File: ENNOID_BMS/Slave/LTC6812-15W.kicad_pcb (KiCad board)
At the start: 2 copper layers, 66 x 91.2 mm, 247 parts, among them J1 PB MB 2, J10 PB MB 1, J11 PA MA 1, J2 PA MA 2, J3 Sensors, J5 Cells, J6 Sensors, Q1 DZTT5551, Q10 TSM2323, Q11 TSM2323, Q12 TSM2323, Q13 TSM2323, Q14 TSM2323, Q15 TSM2323, Q16 TSM2323, Q17 DZTT5551, Q18 2N7002, Q19 2N7002, Q2 TSM2323, Q20 2N7002, Q21 2N7002, Q22 2N7002, Q23 2N7002, Q24 2N7002, Q25 2N7002, Q26 2N7002, Q27 2N7002, Q28 2N7002, Q29 2N7002, Q3 TSM2323, Q30 2N7002, Q31 2N7002, Q32 2N7002, Q4 TSM2323, Q5 TSM2323, Q6 TSM2323, Q7 TSM2323, Q8 TSM2323, Q9 TSM2323, U1 LTC6812-1, U2 LTC6812-1

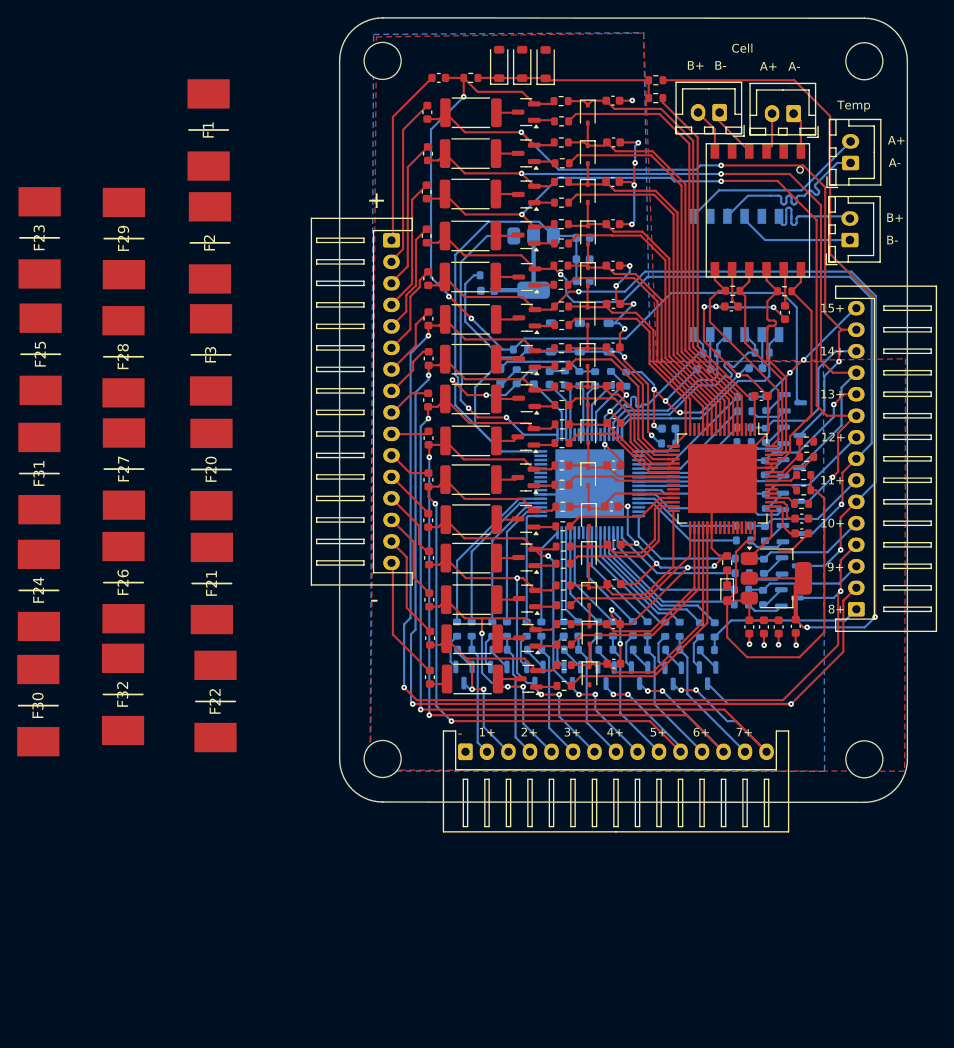
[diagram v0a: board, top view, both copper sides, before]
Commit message: Slave with SMD and no other fuses
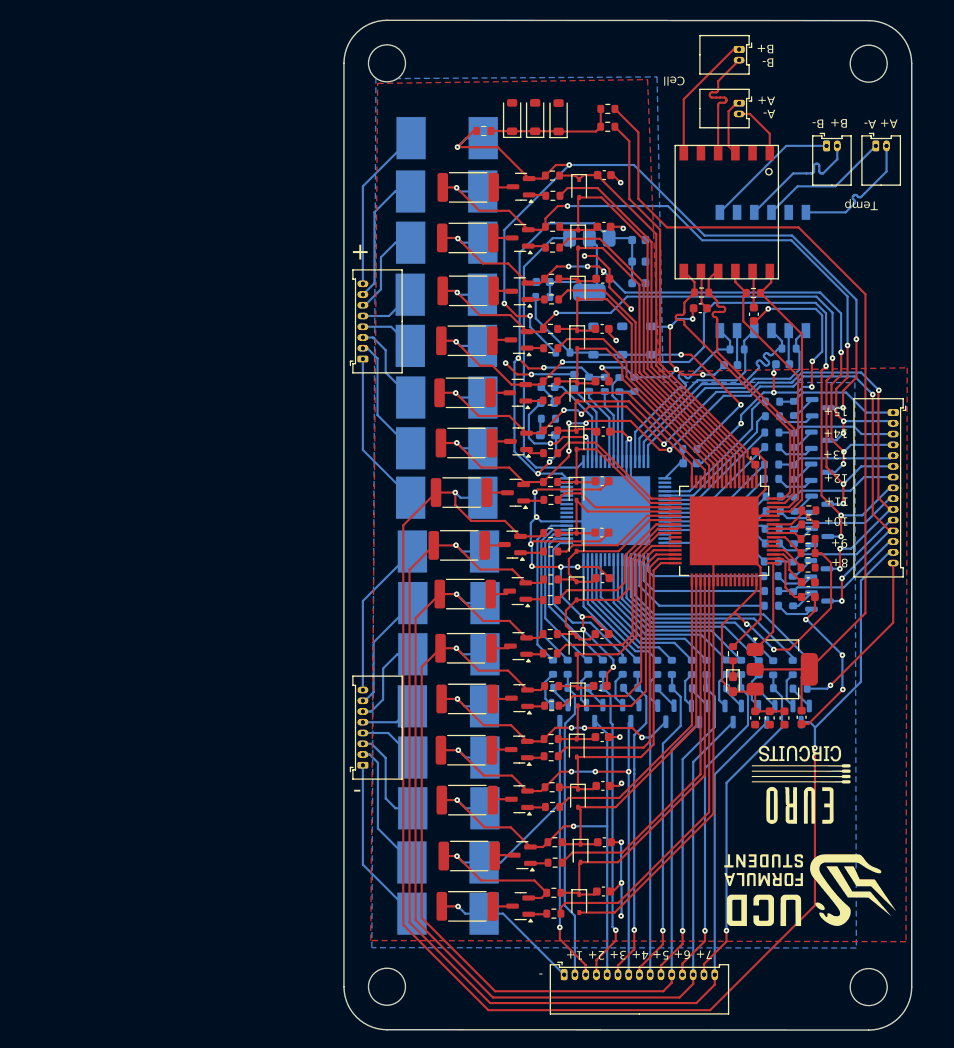
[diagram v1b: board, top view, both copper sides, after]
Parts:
- removed F10, F11, F12, F13, F14, F15, F16, F17, F18, F19, F4, F5, F6, F7, F8, F9: 0.25A, Fuse:Fuse_0603_1608Metric
- added G***: LOGO, LOGO, F.Cu at (99.4, 136.8)
- added G***: LOGO, LOGO, F.Cu at (98.3, 124.3)
- added J4: Conn_01x08, Connector_Molex:Molex_PicoBlade_53048-0810_1x08_P1.25mm_Horizontal, F.Cu at (47.4, 75.0)
- F1, F2, F20, F21, F22, F23, F24, F25, F26, F27, F28, F29, F3, F30, F31, F32: value Fuse -> 5A; moved to B.Cu
- J1, J10, J11, J2: footprint Connector_JST:JST_XH_B2B-XH-A_1x02_P2.50mm_Vertical -> Connector_Molex:Molex_PicoBlade_53048-0210_1x02_P1.25mm_Horizontal
- J3, J6: footprint Connector_JST:JST_XH_S15B-XH-A_1x15_P2.50mm_Horizontal -> Connector_Molex:Molex_PicoBlade_53048-1510_1x15_P1.25mm_Horizontal
- J5: value Cells -> Conn_01x08; footprint Connector_JST:JST_XH_S16B-XH-A_1x16_P2.50mm_Horizontal -> Connector_Molex:Molex_PicoBlade_53048-0810_1x08_P1.25mm_Horizontal
- moved F29 71.2 mm to (57.4, 121.3), turned to 0 degrees
- moved F31 65.6 mm to (57.2, 133.5), turned to 0 degrees
- moved J5 61.1 mm to (47.4, 122.2), turned to 90 degrees
- moved F28 55.5 mm to (57.3, 115.4), turned to 0 degrees
- moved F23 53.3 mm to (57.1, 85.4), turned to 0 degrees
- moved F25 52.7 mm to (57.3, 97.4), turned to 0 degrees
- moved F30 49.2 mm to (57.4, 127.2), turned to 0 degrees
- moved F24 48.6 mm to (57.1, 91.1), turned to 0 degrees
- moved F32 45.6 mm to (57.3, 139.5), turned to 0 degrees
- moved F22 44.4 mm to (57.1, 79.5), turned to 0 degrees
- moved F27 43.5 mm to (57.4, 109.3), turned to 0 degrees
- moved F21 38.8 mm to (57.1, 73.5), turned to 0 degrees
- moved F26 37.9 mm to (57.4, 103.4), turned to 0 degrees
- moved F20 34.0 mm to (57.1, 67.5), turned to 0 degrees
- moved F3 30.4 mm to (57.1, 61.5), turned to 0 degrees
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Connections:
- F1 pad 1: unconnected-(F1-Pad1) -> Net-(J4-Pin_8)
- F1 pad 2: unconnected-(F1-Pad2) -> Cell_15+
- F2 pad 1: unconnected-(F2-Pad1) -> Net-(J4-Pin_7)
- F2 pad 2: unconnected-(F2-Pad2) -> Cell_14+
- F20 pad 1: unconnected-(F20-Pad1) -> Net-(J4-Pin_5)
- F20 pad 2: unconnected-(F20-Pad2) -> Cell_12+
- F21 pad 1: unconnected-(F21-Pad1) -> Net-(J4-Pin_4)
- F21 pad 2: unconnected-(F21-Pad2) -> Cell_11+
- F22 pad 1: unconnected-(F22-Pad1) -> Net-(J4-Pin_3)
- F22 pad 2: unconnected-(F22-Pad2) -> Cell_10+
- F23 pad 1: unconnected-(F23-Pad1) -> Net-(J4-Pin_2)
- F23 pad 2: unconnected-(F23-Pad2) -> Cell_9+
- F24 pad 1: unconnected-(F24-Pad1) -> Net-(J4-Pin_1)
- F24 pad 2: unconnected-(F24-Pad2) -> Cell_8+
- F25 pad 1: unconnected-(F25-Pad1) -> Net-(J5-Pin_8)
- F25 pad 2: unconnected-(F25-Pad2) -> Cell_7+
- F26 pad 1: unconnected-(F26-Pad1) -> Net-(J5-Pin_7)
- F26 pad 2: unconnected-(F26-Pad2) -> Cell_6+
- F27 pad 1: unconnected-(F27-Pad1) -> Net-(J5-Pin_6)
- F27 pad 2: unconnected-(F27-Pad2) -> Cell_5+
- F28 pad 1: unconnected-(F28-Pad1) -> Net-(J5-Pin_5)
- F28 pad 2: unconnected-(F28-Pad2) -> Cell_4+
- F29 pad 1: unconnected-(F29-Pad1) -> Net-(J5-Pin_4)
- F29 pad 2: unconnected-(F29-Pad2) -> Cell_3+
- F3 pad 1: unconnected-(F3-Pad1) -> Net-(J4-Pin_6)
- F3 pad 2: unconnected-(F3-Pad2) -> Cell_13+
- F30 pad 1: unconnected-(F30-Pad1) -> Net-(J5-Pin_3)
- F30 pad 2: unconnected-(F30-Pad2) -> Cell_2+
- F31 pad 1: unconnected-(F31-Pad1) -> Net-(J5-Pin_2)
- F31 pad 2: unconnected-(F31-Pad2) -> Cell_1+
- F32 pad 1: unconnected-(F32-Pad1) -> Net-(J5-Pin_1)
- F32 pad 2: unconnected-(F32-Pad2) -> Cell_1-
- J1 pad 1: ISO_2A_N -> ISO_2B_N
- J1 pad 2: ISO_2A_P -> ISO_2B_P
- J10 pad 1: ISO_1A_N -> ISO_1A_P
- J10 pad 2: ISO_1A_P -> ISO_1A_N
- J11 pad 1: ISO_1B_N -> ISO_1B_P
- J11 pad 2: ISO_1B_P -> ISO_1B_N
- J2 pad 1: ISO_2B_P -> ISO_2A_N
- J2 pad 2: ISO_2B_N -> ISO_2A_P
- J3 pad 1: Meas8+ -> Meas15+
- J3 pad 10: Cell_12+ -> Cell_10+
- J3 pad 11: Meas13+ -> Meas10+
- J3 pad 12: Cell_13+ -> Cell_9+
- J3 pad 13: Meas14+ -> Meas9+
- J3 pad 14: Cell_14+ -> Cell_8+
- J3 pad 15: Meas15+ -> Meas8+
- J3 pad 2: Cell_8+ -> Cell_14+
- J3 pad 3: Meas9+ -> Meas14+
- J3 pad 4: Cell_9+ -> Cell_13+
- J3 pad 5: Meas10+ -> Meas13+
- J3 pad 6: Cell_10+ -> Cell_12+
- J3 pad 7: Meas11+ -> Meas12+
- J3 pad 9: Meas12+ -> Meas11+
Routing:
- net Cell_1-: track 211.9 -> 328.5 mm, vias 33 -> 37
- net Cell_8+: track 128.3 -> 177.3 mm, vias 3 -> 2
- net Cell_9+: track 131.4 -> 96.9 mm, vias 3 -> 8
- net Cell_1+: track 31.7 -> 64.1 mm
- net Cell_6+: track 97.1 -> 126.1 mm, vias 4 -> 1
- net Cell_5+: track 85.8 -> 114.8 mm, vias 4 -> 1
- net Cell_7+: track 108.7 -> 136.6 mm, vias 4 -> 1
- net Meas6+: track 16.1 -> 38.4 mm, vias 0 -> 1
- net Meas5+: track 15.7 -> 37.9 mm, vias 0 -> 1
- net Meas7+: track 17.0 -> 39.0 mm, vias 0 -> 1
- net Meas4+: track 15.3 -> 37.3 mm, vias 0 -> 1
- net Meas1+: track 14.3 -> 36.3 mm
- net Meas2+: track 14.7 -> 36.5 mm, vias 0 -> 1
- net Meas3+: track 15.3 -> 36.7 mm, vias 0 -> 1
- net /cell1/S: track 29.9 -> 49.5 mm
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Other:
- board size 66 x 91.2 mm -> 66 x 117.4 mm

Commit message: fused slave variant v1
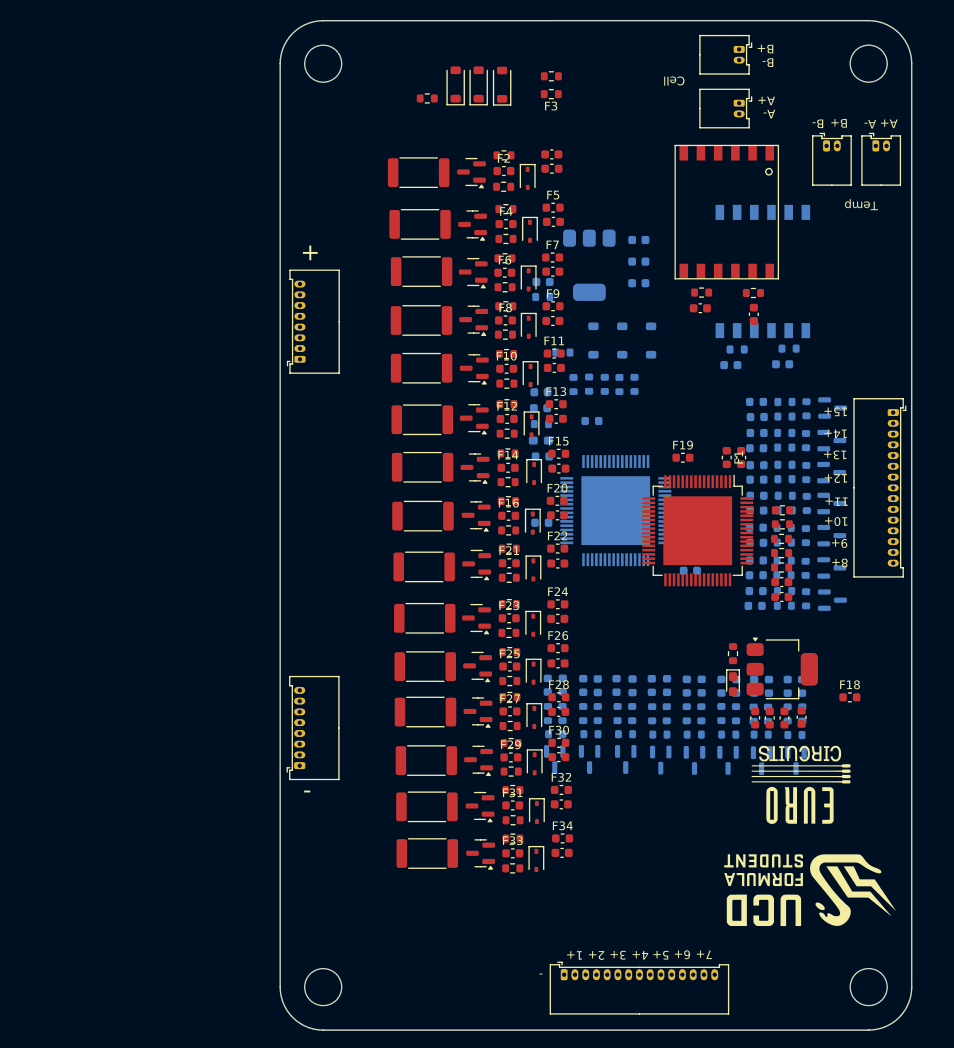
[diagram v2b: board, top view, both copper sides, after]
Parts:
- added F10: 50mA, Fuse:Fuse_0603_1608Metric, F.Cu at (64.1, 76.1)
- added F11: 50mA, Fuse:Fuse_0603_1608Metric, F.Cu at (69.6, 74.4)
- added F12: 50mA, Fuse:Fuse_0603_1608Metric, F.Cu at (64.1, 82.0)
- added F13: 50mA, Fuse:Fuse_0603_1608Metric, F.Cu at (69.8, 80.3)
- added F14: 50mA, Fuse:Fuse_0603_1608Metric, F.Cu at (64.2, 87.7)
- added F15: 50mA, Fuse:Fuse_0603_1608Metric, F.Cu at (70.1, 86.0)
- added F16: 50mA, Fuse:Fuse_0603_1608Metric, F.Cu at (64.3, 93.2)
- added F17: 50mA, Fuse:Fuse_0603_1608Metric, B.Cu at (93.1, 100.1)
- added F18: 50mA, Fuse:Fuse_0603_1608Metric, F.Cu at (104.0, 114.3)
- added F19: 50mA, Fuse:Fuse_0603_1608Metric, F.Cu at (84.6, 86.5)
- added F33: 50mA, Fuse:Fuse_0603_1608Metric, F.Cu at (64.8, 132.5)
- added F34: 50mA, Fuse:Fuse_0603_1608Metric, F.Cu at (70.6, 130.7)
- added F35: 50mA, Fuse:Fuse_0603_1608Metric, B.Cu at (93.1, 102.0)
- added F36: 50mA, Fuse:Fuse_0603_1608Metric, B.Cu at (93.0, 103.7)
- added F37: 50mA, Fuse:Fuse_0603_1608Metric, B.Cu at (98.4, 113.1)
- added F38: 50mA, Fuse:Fuse_0603_1608Metric, B.Cu at (96.7, 113.1)
- added F39: 50mA, Fuse:Fuse_0603_1608Metric, B.Cu at (94.6, 113.1)
- added F4: 50mA, Fuse:Fuse_0603_1608Metric, F.Cu at (64.0, 59.3)
- added F40: 50mA, Fuse:Fuse_0603_1608Metric, B.Cu at (92.8, 113.0)
- added F41: 50mA, Fuse:Fuse_0603_1608Metric, B.Cu at (90.8, 113.0)
- added F42: 50mA, Fuse:Fuse_0603_1608Metric, B.Cu at (89.0, 113.0)
- added F43: 50mA, Fuse:Fuse_0603_1608Metric, B.Cu at (85.0, 113.0)
- added F44: 50mA, Fuse:Fuse_0603_1608Metric, B.Cu at (82.7, 113.0)
- added F45: 50mA, Fuse:Fuse_0603_1608Metric, B.Cu at (80.9, 113.0)
- added F46: 50mA, Fuse:Fuse_0603_1608Metric, B.Cu at (78.7, 113.0)
- added F47: 50mA, Fuse:Fuse_0603_1608Metric, B.Cu at (86.7, 113.0)
- added F48: 50mA, Fuse:Fuse_0603_1608Metric, B.Cu at (76.8, 113.0)
- added F49: 50mA, Fuse:Fuse_0603_1608Metric, B.Cu at (74.7, 113.0)
- added F5: 50mA, Fuse:Fuse_0603_1608Metric, F.Cu at (69.5, 57.4)
- added F50: 50mA, Fuse:Fuse_0603_1608Metric, B.Cu at (73.0, 113.0)
- added F51: 50mA, Fuse:Fuse_0603_1608Metric, B.Cu at (70.6, 112.9)
- added F52: 50mA, Fuse:Fuse_0603_1608Metric, B.Cu at (68.8, 112.9)
- added F53: 50mA, Fuse:Fuse_0603_1608Metric, B.Cu at (68.2, 94.0)
- added F54: 50mA, Fuse:Fuse_0603_1608Metric, B.Cu at (93.1, 96.4)
- added F55: 50mA, Fuse:Fuse_0603_1608Metric, B.Cu at (93.1, 94.6)
- added F56: 50mA, Fuse:Fuse_0603_1608Metric, B.Cu at (93.2, 92.6)
- added F57: 50mA, Fuse:Fuse_0603_1608Metric, B.Cu at (93.2, 90.9)
- added F58: 50mA, Fuse:Fuse_0603_1608Metric, B.Cu at (93.2, 89.0)
- added F59: 50mA, Fuse:Fuse_0603_1608Metric, B.Cu at (93.2, 87.3)
- added F6: 50mA, Fuse:Fuse_0603_1608Metric, F.Cu at (63.9, 65.0)
- added F60: 50mA, Fuse:Fuse_0603_1608Metric, B.Cu at (93.1, 85.4)
- added F61: 50mA, Fuse:Fuse_0603_1608Metric, B.Cu at (93.2, 83.6)
- added F62: 50mA, Fuse:Fuse_0603_1608Metric, B.Cu at (93.2, 81.8)
- added F63: 50mA, Fuse:Fuse_0603_1608Metric, B.Cu at (93.1, 80.0)
- added F64: 50mA, Fuse:Fuse_0603_1608Metric, B.Cu at (93.1, 98.4)
- added F65: 50mA, Fuse:Fuse_0603_1608Metric, B.Cu at (74.0, 82.2)
- added F66: 50mA, Fuse:Fuse_0603_1608Metric, B.Cu at (68.2, 86.3)
- added F67: 50mA, Fuse:Fuse_0603_1608Metric, B.Cu at (85.4, 96.0)
- added F7: 50mA, Fuse:Fuse_0603_1608Metric, F.Cu at (69.4, 63.2)
- added F8: 50mA, Fuse:Fuse_0603_1608Metric, F.Cu at (63.9, 70.5)
- added F9: 50mA, Fuse:Fuse_0603_1608Metric, F.Cu at (69.5, 68.9)
- F1, F2, F20, F21, F22, F23, F24, F25, F26, F27, F28, F29, F3, F30, F31, F32: value 5A -> 50mA; footprint ENNOID:FUSC10948X488N -> Fuse:Fuse_0603_1608Metric; moved to F.Cu
- moved F1 49.3 mm to (89.7, 86.5), turned to -90 degrees
- moved F20 27.2 mm to (70.0, 91.5)
- moved F21 26.3 mm to (64.4, 98.8)
- moved F22 21.8 mm to (70.0, 97.0)
- moved F23 21.1 mm to (64.4, 105.1)
- moved F32 19.5 mm to (70.4, 125.1)
- moved F24 17.9 mm to (70.0, 103.5)
- moved F25 15.2 mm to (64.4, 110.8)
- moved F3 14.9 mm to (69.3, 52.9)
- moved F30 14.9 mm to (70.1, 119.6)
- moved F26 13.7 mm to (70.0, 108.6)
- moved F28 12.9 mm to (70.1, 114.3)
- moved C10 12.5 mm to (85.4, 99.6)
- moved R74 12.5 mm to (85.4, 98.0)
- moved F31 10.0 mm to (64.8, 126.9)
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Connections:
- C1 pad 2: Net-(U1-V+) -> Net-(C1-Pad2)
- C10 pad 2: Net-(U2-V+) -> Net-(C10-Pad2)
- C11 pad 2: /cell1/C -> Net-(D5-K)
- C12 pad 2: /cell2/C -> Net-(D6-K)
- C13 pad 2: /cell3/C -> Net-(D7-K)
- C14 pad 2: /cell4/C -> Net-(D8-K)
- C15 pad 2: /cell5/C -> Net-(D9-K)
- C16 pad 2: /cell6/C -> Net-(D10-K)
- C17 pad 2: /cell7/C -> Net-(D11-K)
- C18 pad 2: /cell8/C -> Net-(D12-K)
- C19 pad 2: /cell10/CM -> Net-(D13-K)
- C20 pad 2: /cell10/C -> Net-(D14-K)
- C21 pad 2: /cell11/C -> Net-(D15-K)
- C22 pad 2: /cell12/C -> Net-(D16-K)
- C23 pad 2: /cell13/C -> Net-(D17-K)
- C24 pad 2: /cell14/C -> Net-(D18-K)
- C25 pad 2: /cell15/C -> Net-(D19-K)
- C29 pad 2: /Vreg_2 -> Net-(Q17-E)
- C30 pad 2: /Vreg_2 -> Net-(Q17-E)
- C31 pad 2: /Vreg_2 -> Net-(Q17-E)
- C5 pad 2: /Vreg_1 -> Net-(Q1-E)
- C6 pad 2: /Vreg_1 -> Net-(Q1-E)
- C7 pad 2: /Vreg_1 -> Net-(Q1-E)
- D10 pad 1: /cell6/C -> Net-(D10-K)
- D11 pad 1: /cell7/C -> Net-(D11-K)
- D12 pad 1: /cell8/C -> Net-(D12-K)
- D13 pad 1: /cell10/CM -> Net-(D13-K)
- D14 pad 1: /cell10/C -> Net-(D14-K)
- D15 pad 1: /cell11/C -> Net-(D15-K)
- D16 pad 1: /cell12/C -> Net-(D16-K)
- D17 pad 1: /cell13/C -> Net-(D17-K)
- D18 pad 1: /cell14/C -> Net-(D18-K)
- D19 pad 1: /cell15/C -> Net-(D19-K)
- D5 pad 1: /cell1/C -> Net-(D5-K)
- D6 pad 1: /cell2/C -> Net-(D6-K)
- D7 pad 1: /cell3/C -> Net-(D7-K)
- D8 pad 1: /cell4/C -> Net-(D8-K)
- D9 pad 1: /cell5/C -> Net-(D9-K)
- F1 pad 1: Net-(J4-Pin_8) -> Net-(C1-Pad2)
- F1 pad 2: Cell_15+ -> Net-(U1-V+)
- F2 pad 1: Net-(J4-Pin_7) -> Net-(F2-Pad1)
- F2 pad 2: Cell_14+ -> /cell15/S
- F20 pad 1: Net-(J4-Pin_5) -> Net-(D12-K)
- F20 pad 2: Cell_12+ -> /cell8/C
- F21 pad 1: Net-(J4-Pin_4) -> Net-(F21-Pad1)
- F21 pad 2: Cell_11+ -> /cell7/S
- F22 pad 1: Net-(J4-Pin_3) -> Net-(D11-K)
- F22 pad 2: Cell_10+ -> /cell7/C
- F23 pad 1: Net-(J4-Pin_2) -> Net-(F23-Pad1)
- F23 pad 2: Cell_9+ -> /cell6/S
- F24 pad 1: Net-(J4-Pin_1) -> Net-(D10-K)
- F24 pad 2: Cell_8+ -> /cell6/C
- F25 pad 1: Net-(J5-Pin_8) -> Net-(F25-Pad1)
- F25 pad 2: Cell_7+ -> /cell5/S
- F26 pad 1: Net-(J5-Pin_7) -> Net-(D9-K)
- F26 pad 2: Cell_6+ -> /cell5/C
- F27 pad 1: Net-(J5-Pin_6) -> Net-(F27-Pad1)
- F27 pad 2: Cell_5+ -> /cell4/S
- F28 pad 1: Net-(J5-Pin_5) -> Net-(D8-K)
- F28 pad 2: Cell_4+ -> /cell4/C
- F29 pad 1: Net-(J5-Pin_4) -> Net-(F29-Pad1)
- F29 pad 2: Cell_3+ -> /cell3/S
- F3 pad 1: Net-(J4-Pin_6) -> Net-(D19-K)
- F3 pad 2: Cell_13+ -> /cell15/C
- F30 pad 1: Net-(J5-Pin_3) -> Net-(D7-K)
- F30 pad 2: Cell_2+ -> /cell3/C
- F31 pad 1: Net-(J5-Pin_2) -> Net-(F31-Pad1)
- F31 pad 2: Cell_1+ -> /cell2/S
- F32 pad 1: Net-(J5-Pin_1) -> Net-(D6-K)
- F32 pad 2: Cell_1- -> /cell2/C
- J4 pad 1: Net-(J4-Pin_1) -> Cell_8+
- J4 pad 2: Net-(J4-Pin_2) -> Cell_9+
- J4 pad 3: Net-(J4-Pin_3) -> Cell_10+
- J4 pad 4: Net-(J4-Pin_4) -> Cell_11+
- J4 pad 5: Net-(J4-Pin_5) -> Cell_12+
- J4 pad 6: Net-(J4-Pin_6) -> Cell_13+
- J4 pad 7: Net-(J4-Pin_7) -> Cell_14+
- J4 pad 8: Net-(J4-Pin_8) -> Cell_15+
- J5 pad 1: Net-(J5-Pin_1) -> Cell_1-
- J5 pad 2: Net-(J5-Pin_2) -> Cell_1+
- J5 pad 3: Net-(J5-Pin_3) -> Cell_2+
- J5 pad 4: Net-(J5-Pin_4) -> Cell_3+
- J5 pad 5: Net-(J5-Pin_5) -> Cell_4+
- J5 pad 6: Net-(J5-Pin_6) -> Cell_5+
- J5 pad 7: Net-(J5-Pin_7) -> Cell_6+
- J5 pad 8: Net-(J5-Pin_8) -> Cell_7+
- Q1 pad 3: /Vreg_1 -> Net-(Q1-E)
- Q17 pad 3: /Vreg_2 -> Net-(Q17-E)
- R1 pad 1: Net-(U1-V+) -> Net-(C1-Pad2)
- R14 pad 1: /cell1/S -> Net-(F33-Pad1)
- R15 pad 1: /cell1/C -> Net-(D5-K)
- R18 pad 1: /cell2/S -> Net-(F31-Pad1)
- R19 pad 1: /cell2/C -> Net-(D6-K)
- R22 pad 1: /cell3/S -> Net-(F29-Pad1)
- R23 pad 1: /cell3/C -> Net-(D7-K)
- R26 pad 1: /cell4/S -> Net-(F27-Pad1)
- R27 pad 1: /cell4/C -> Net-(D8-K)
- R30 pad 1: /cell5/S -> Net-(F25-Pad1)
- R31 pad 1: /cell5/C -> Net-(D9-K)
- R34 pad 1: /cell6/S -> Net-(F23-Pad1)
- R35 pad 1: /cell6/C -> Net-(D10-K)
- R38 pad 1: /cell7/S -> Net-(F21-Pad1)
- R39 pad 1: /cell7/C -> Net-(D11-K)
- R42 pad 1: /cell8/S -> Net-(F16-Pad1)
- R43 pad 1: /cell8/C -> Net-(D12-K)
- R46 pad 1: /cell9/S -> Net-(F14-Pad1)
- R47 pad 1: /cell10/CM -> Net-(D13-K)
- R50 pad 1: /cell10/S -> Net-(F12-Pad1)
- R51 pad 1: /cell10/C -> Net-(D14-K)
- R54 pad 1: /cell11/S -> Net-(F10-Pad1)
- R55 pad 1: /cell11/C -> Net-(D15-K)
- R58 pad 1: /cell12/S -> Net-(F8-Pad1)
- R59 pad 1: /cell12/C -> Net-(D16-K)
- R62 pad 1: /cell13/S -> Net-(F6-Pad1)
- R63 pad 1: /cell13/C -> Net-(D17-K)
- R66 pad 1: /cell14/S -> Net-(F4-Pad1)
- R67 pad 1: /cell14/C -> Net-(D18-K)
- R70 pad 1: /cell15/S -> Net-(F2-Pad1)
- R71 pad 1: /cell15/C -> Net-(D19-K)
- R74 pad 1: Net-(U2-V+) -> Net-(C10-Pad2)
- R84 pad 1: Net-(U2-C15) -> Net-(F63-Pad1)
- R85 pad 1: Net-(U2-C14) -> Net-(F61-Pad1)
- R86 pad 1: Net-(U2-C13) -> Net-(F59-Pad1)
- R87 pad 1: Net-(U2-C12) -> Net-(F57-Pad1)
- R88 pad 1: Net-(U2-C11) -> Net-(F55-Pad1)
- R89 pad 1: Net-(U2-C10) -> Net-(F64-Pad1)
- R90 pad 1: Net-(U2-C9) -> Net-(F35-Pad2)
- R91 pad 1: Net-(U2-C8) -> Net-(F37-Pad2)
- R92 pad 1: Net-(U2-C7) -> Net-(F39-Pad2)
- R93 pad 1: Net-(U2-C6) -> Net-(F41-Pad2)
- R94 pad 1: Net-(U2-C5) -> Net-(F47-Pad2)
- R95 pad 1: Net-(U2-C4) -> Net-(F44-Pad2)
- R96 pad 1: Net-(U2-C3) -> Net-(F46-Pad2)
- R98 pad 2: Net-(U2-C1) -> Net-(F51-Pad2)
- R99 pad 2: Net-(U2-C2) -> Net-(F49-Pad2)
- U1 pad 39: /T1 -> unconnected-(U1-GPIO1-Pad39)
- U1 pad 65: Cell_1- -> Net-(U1-V-)
- U2 pad 11: S12 -> Net-(U2-S12)
- U2 pad 13: S11 -> Net-(U2-S11)
- U2 pad 17: S10 -> Net-(U2-S10)
- U2 pad 19: S9 -> Net-(U2-S9)
- U2 pad 21: S8 -> Net-(U2-S8)
- U2 pad 23: S7 -> Net-(U2-S7)
- U2 pad 25: S6 -> Net-(U2-S6)
- U2 pad 29: S5 -> Net-(U2-S5)
- U2 pad 31: S4 -> Net-(U2-S4)
- U2 pad 33: S3 -> Net-(U2-S3)
- U2 pad 35: S2 -> Net-(U2-S2)
- U2 pad 37: S1 -> Net-(U2-S1)
- U2 pad 38: Cell_1- -> Net-(U2-C0)
- U2 pad 5: S15 -> Net-(U2-S15)
- U2 pad 65: Cell_1- -> Net-(U2-V-)
- U2 pad 7: S14 -> Net-(U2-S14)
- U2 pad 9: S13 -> Net-(U2-S13)
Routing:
- net Cell_1-: track 328.5 -> 0.00 mm, vias 37 -> 0
- net Cell_8+: track 177.3 -> 0.00 mm, vias 2 -> 0
- net Cell_7+: track 136.6 -> 0.00 mm, vias 1 -> 0
- net Cell_6+: track 126.1 -> 0.00 mm, vias 1 -> 0
- net Cell_5+: track 114.8 -> 0.00 mm, vias 1 -> 0
- net Cell_15+: track 104.7 -> 0.00 mm, vias 6 -> 0
- net Net-(C4-Pad2): track 100.3 -> 0.00 mm
- net Cell_9+: track 96.9 -> 0.00 mm, vias 8 -> 0
- net Cell_11+: track 92.9 -> 0.00 mm, vias 5 -> 0
- net Cell_10+: track 90.9 -> 0.00 mm, vias 7 -> 0
- net Cell_12+: track 84.8 -> 0.00 mm, vias 5 -> 0
- net Cell_14+: track 83.3 -> 0.00 mm, vias 5 -> 0
- net Cell_13+: track 81.6 -> 0.00 mm, vias 7 -> 0
- net /Vreg_2: track 67.7 -> 0.00 mm, vias 4 -> 0
- net Cell_1+: track 64.1 -> 0.00 mm, vias 2 -> 0
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- removed copper zone on B.Cu, net Cell_1-
- removed copper zone on F.Cu, net Cell_1-
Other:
- board size 66 x 117.4 mm -> 73.4 x 117.4 mm

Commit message: fuse boards
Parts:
- removed F10, F12, F14, F16, F17, F2, F21, F23, F25, F27, F29, F31, F33, F36, F38, F4, F40, F42, F43, F45, F48, F50, F52, F54, F56, F58, F6, F60, F62, F8: 50mA, Fuse:Fuse_0603_1608Metric
- R100, R101, R102, R103, R104, R105, R106, R107, R108, R109, R110, R14, R18, R22, R26, R30, R34, R38, R42, R46, R50, R54, R58, R62, R66, R68, R70, R72, R73, R97: footprint Resistor_SMD:R_0603_1608Metric -> Resistor_SMD:R_0508_1220Metric
- moved C10 22.1 mm to (80.8, 78.0), turned to -90 degrees
- moved R74 20.2 mm to (82.5, 78.0), turned to 90 degrees
- moved F67 18.1 mm to (84.3, 78.0), turned to -90 degrees
- moved F18 17.4 mm to (90.1, 103.8), turned to 90 degrees
- moved R93 9.71 mm to (81.1, 114.9), turned to 0 degrees
- moved R98 9.70 mm to (61.0, 114.8), turned to 180 degrees
- moved R96 9.67 mm to (69.1, 115.0), turned to 0 degrees
- moved F51 9.64 mm to (61.0, 113.2), turned to 180 degrees
- moved F41 9.61 mm to (81.1, 113.1), turned to 180 degrees
- moved R91 9.60 mm to (88.9, 114.9), turned to 0 degrees
- moved F46 9.57 mm to (69.1, 113.3), turned to 180 degrees
- moved R92 9.57 mm to (85.0, 114.9), turned to 0 degrees
- moved F39 9.56 mm to (85.0, 113.2), turned to 180 degrees
- moved R95 9.52 mm to (73.2, 115.0), turned to 0 degrees
- moved R94 9.51 mm to (77.3, 114.9), turned to 0 degrees
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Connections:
- R14 pad 1: Net-(F33-Pad1) -> /cell1/S
- R18 pad 1: Net-(F31-Pad1) -> /cell2/S
- R22 pad 1: Net-(F29-Pad1) -> /cell3/S
- R26 pad 1: Net-(F27-Pad1) -> /cell4/S
- R30 pad 1: Net-(F25-Pad1) -> /cell5/S
- R34 pad 1: Net-(F23-Pad1) -> /cell6/S
- R38 pad 1: Net-(F21-Pad1) -> /cell7/S
- R42 pad 1: Net-(F16-Pad1) -> /cell8/S
- R46 pad 1: Net-(F14-Pad1) -> /cell9/S
- R50 pad 1: Net-(F12-Pad1) -> /cell10/S
- R54 pad 1: Net-(F10-Pad1) -> /cell11/S
- R58 pad 1: Net-(F8-Pad1) -> /cell12/S
- R62 pad 1: Net-(F6-Pad1) -> /cell13/S
- R66 pad 1: Net-(F4-Pad1) -> /cell14/S
- R70 pad 1: Net-(F2-Pad1) -> /cell15/S
- U2 pad 11: Net-(U2-S12) -> S12
- U2 pad 13: Net-(U2-S11) -> S11
- U2 pad 17: Net-(U2-S10) -> S10
- U2 pad 19: Net-(U2-S9) -> S9
- U2 pad 21: Net-(U2-S8) -> S8
- U2 pad 23: Net-(U2-S7) -> S7
- U2 pad 25: Net-(U2-S6) -> S6
- U2 pad 29: Net-(U2-S5) -> S5
- U2 pad 31: Net-(U2-S4) -> S4
- U2 pad 33: Net-(U2-S3) -> S3
- U2 pad 35: Net-(U2-S2) -> S2
- U2 pad 37: Net-(U2-S1) -> S1
- U2 pad 5: Net-(U2-S15) -> S15
- U2 pad 7: Net-(U2-S14) -> S14
- U2 pad 9: Net-(U2-S13) -> S13
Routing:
- net Cell_9+: track 0.00 -> 204.3 mm, vias 0 -> 2
- net Cell_8+: track 0.00 -> 152.6 mm, vias 0 -> 5
- net Cell_15+: track 0.00 -> 141.7 mm, vias 0 -> 5
- net Cell_10+: track 0.00 -> 133.0 mm, vias 0 -> 4
- net Cell_11+: track 0.00 -> 129.3 mm, vias 0 -> 3
- net Cell_7+: track 0.00 -> 128.0 mm, vias 0 -> 2
- net Cell_6+: track 0.00 -> 123.2 mm, vias 0 -> 2
- net Cell_5+: track 0.00 -> 116.1 mm, vias 0 -> 2
- net Cell_4+: track 0.00 -> 109.6 mm, vias 0 -> 2
- net Cell_13+: track 0.00 -> 108.7 mm, vias 0 -> 3
- net Cell_14+: track 0.00 -> 108.7 mm, vias 0 -> 3
- net Cell_3+: track 0.00 -> 106.7 mm, vias 0 -> 2
- net Cell_2+: track 0.00 -> 104.3 mm, vias 0 -> 2
- net Cell_1+: track 0.00 -> 104.0 mm, vias 0 -> 2
- net Cell_12+: track 0.00 -> 100.7 mm, vias 0 -> 3
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- added copper zone on B.Cu, net Cell_1-
- added copper zone on F.Cu, net Cell_1-
